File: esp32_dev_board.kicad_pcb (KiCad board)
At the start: 4 copper layers, 26.4 x 67.6 mm, 27 parts, among them J1 USB_B_Micro, J2 Conn_01x12, J3 Conn_01x12, Q1 Q_PMOS_GSD, Q2 MBT3904DW1, SW1 SW_Push, U1 ESP32-WROOM-32, U2 AP2112K-3.3, U3 FT231XS

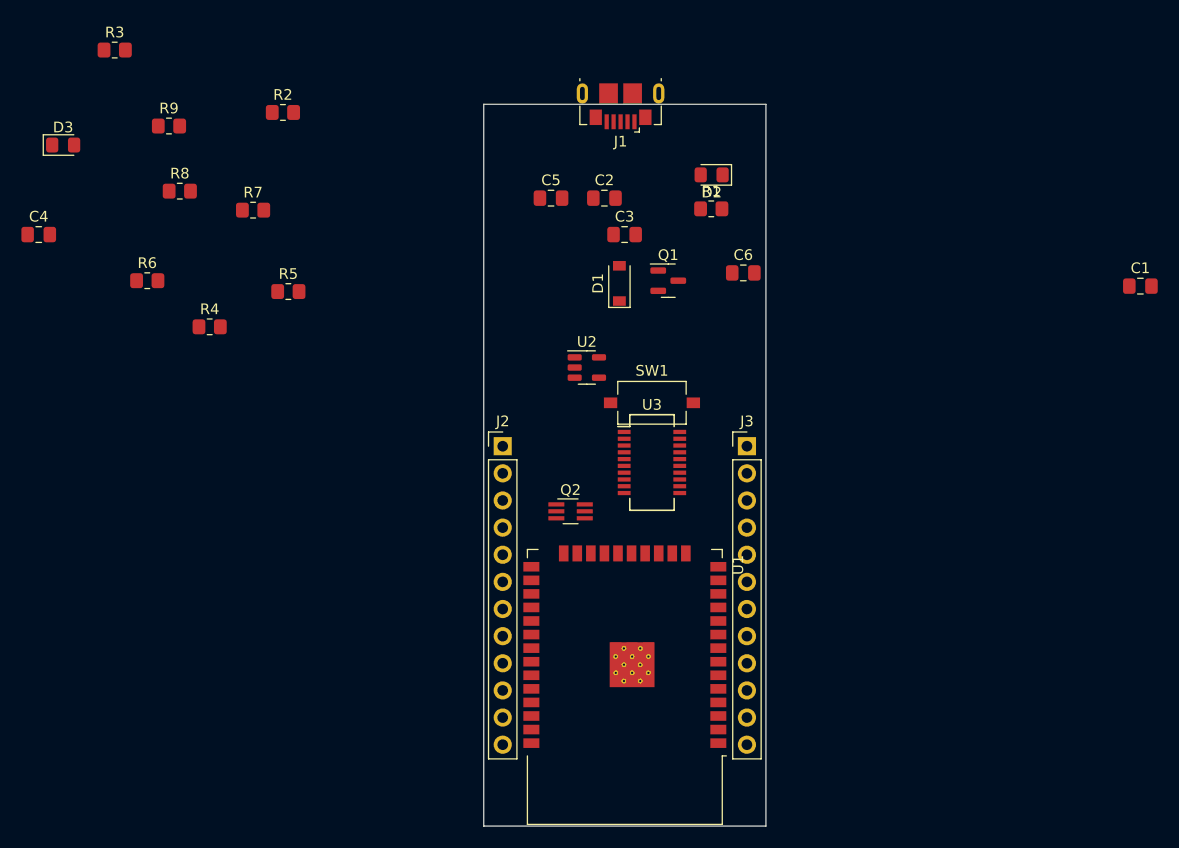
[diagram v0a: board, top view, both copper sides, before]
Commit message: Change to 4-layer board and finish routing
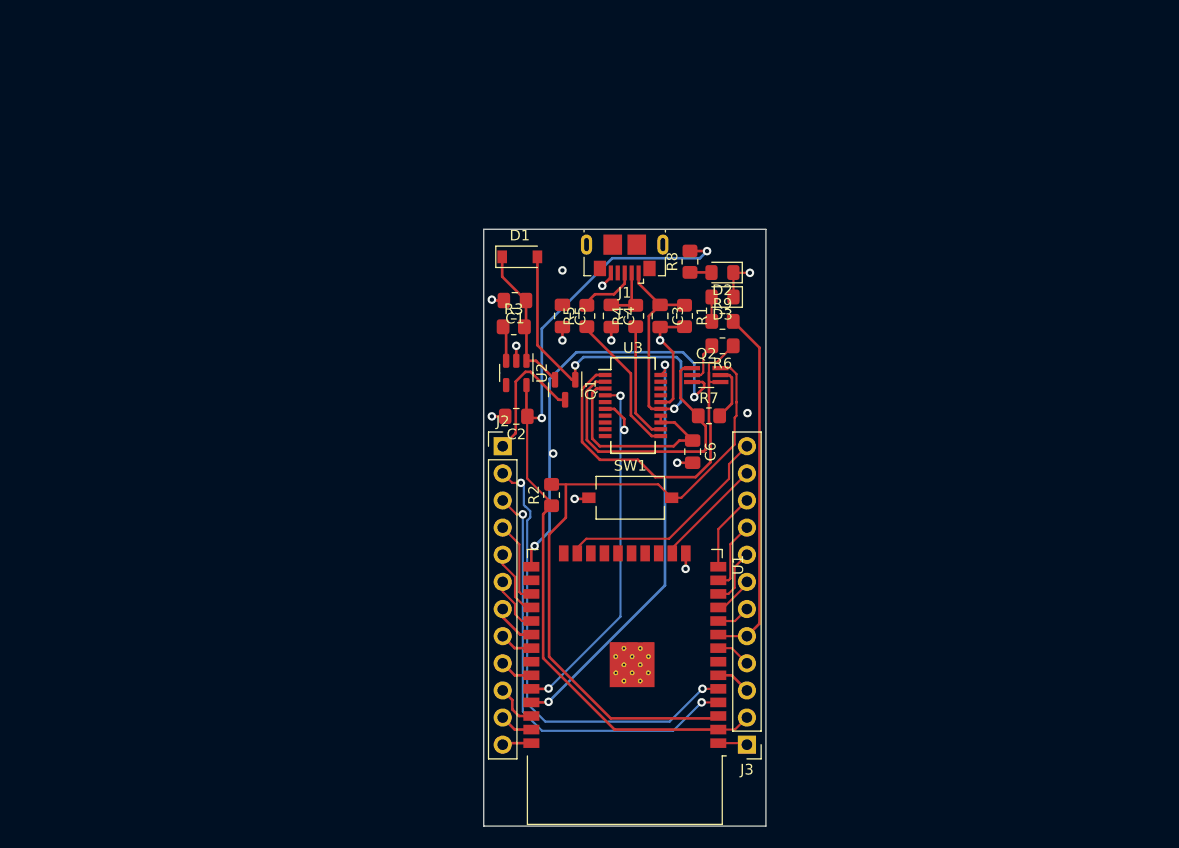
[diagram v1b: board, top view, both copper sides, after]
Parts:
- moved D3 63.3 mm to (178.1, 95.2), turned to 180 degrees
- moved C1 58.6 mm to (158.6, 95.6), turned to 180 degrees
- moved R9 54.9 mm to (178.1, 97.5)
- moved R6 54.2 mm to (178.1, 99.8), turned to 180 degrees
- moved C4 54.1 mm to (167.6, 97.0), turned to -90 degrees
- moved R8 48.2 mm to (175.0, 91.9), turned to 90 degrees
- moved R7 46.8 mm to (176.8, 106.4)
- moved R3 45.5 mm to (158.5, 98.0)
- moved R2 43.8 mm to (162.1, 113.8), turned to 90 degrees
- moved R4 39.9 mm to (169.9, 97.0), turned to 90 degrees
- moved R5 28.0 mm to (165.4, 97.0), turned to 90 degrees
- moved J3 27.9 mm to (180.3, 137.2), turned to 180 degrees
- moved C2 22.0 mm to (158.8, 106.4), turned to 180 degrees
- moved Q2 18.0 mm to (176.5, 102.6)
- moved C6 17.4 mm to (175.3, 109.7), turned to -90 degrees
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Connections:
- U3 pad 20: TX -> TX0
- U3 pad 4: RX -> RX0
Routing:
- net +3.3V: track 0.00 -> 79.0 mm, vias 0 -> 2
- net CHIP_PU: track 0.00 -> 63.3 mm
- net VBUS: track 0.00 -> 48.1 mm, vias 0 -> 2
- net A3: track 0.00 -> 43.1 mm, vias 0 -> 2
- net A4: track 0.00 -> 41.0 mm, vias 0 -> 2
- net GPIO0: track 0.00 -> 39.3 mm, vias 0 -> 2
- net TX0: track 0.00 -> 38.8 mm, vias 0 -> 2
- net DTR: track 0.00 -> 35.8 mm
- net GND: track 0.00 -> 35.5 mm, vias 0 -> 15
- net GPIO33: track 0.00 -> 33.7 mm
- net RX0: track 0.00 -> 33.3 mm, vias 0 -> 2
- net RTS: track 0.00 -> 27.8 mm
- net MTDO: track 0.00 -> 21.2 mm
- net Net-(C6-Pad1): track 0.00 -> 19.9 mm
- net Net-(C1-Pad1): track 0.00 -> 14.2 mm
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- added copper zone on In1.Cu, net GND
- added copper zone on In2.Cu, net GND
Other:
- board size 26.4 x 67.6 mm -> 26.4 x 55.9 mm

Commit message: Add silkscreen, round corners, and small fixes
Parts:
- added C7: 1uF, Capacitor_SMD:C_0805_2012Metric_Pad1.18x1.45mm_HandSolder, F.Cu at (162.7, 109.4)
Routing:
- net VIN: track 12.6 -> 16.4 mm
- net GND: track 35.5 -> 37.9 mm, vias 15 -> 27
- net Net-(C5-Pad1): track 5.54 -> 7.84 mm
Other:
- board size 26.4 x 55.9 mm -> 25.9 x 55.9 mm
- board text added: "+3.3V"
- board text added: "21"
- board text added: "27"
- board text added: "32"
- board text added: "33"
- board text added: "A0"
- board text added: "A1"
- board text added: "A2"
- board text added: "A3"
- board text added: "A4"
- board text added: "GND"
- board text added: "MISO"
- board text added: "MOSI"
- board text added: "MTCK"
- board text added: "MTDI"
- board text added: "MTDO"
- board text added: "MTMS"
- board text added: "RX2"
- board text added: "SCK"
- board text added: "SCL"
- board text added: "SDA"
- board text added: "TX2"
- board text added: "VIN"

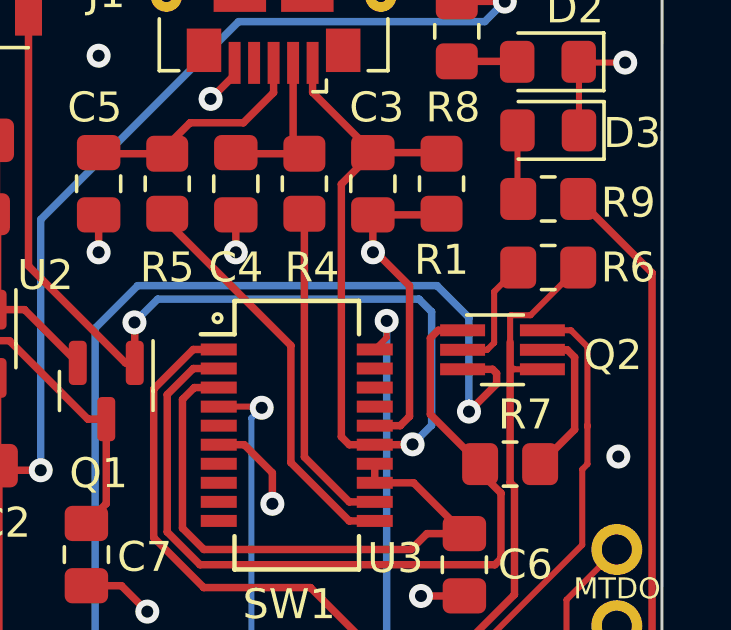
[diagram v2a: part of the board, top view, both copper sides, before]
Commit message: Change C2 value and add back silkscreen
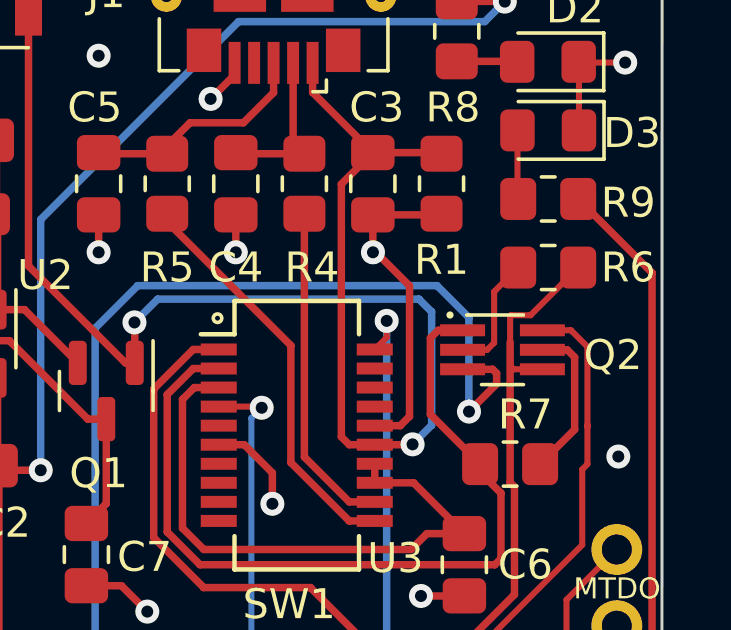
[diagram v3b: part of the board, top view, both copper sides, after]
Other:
- board text added: "Noah White ESP32 Dev Board Rev 1.0"
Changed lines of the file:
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@@
     )
   )
-  (footprint "Package_TO_SOT_SMD:SOT-363_SC-70-6_Handsoldering" placed (layer "F.Cu")
+  (footprint "Package_TO_SOT_SMD:SOT-363_SC-70-6_Handsoldering" (layer "F.Cu")
     (at 176.53 102.563413)
     (descr "SOT-363, SC-70-6, Handsoldering")
@@
       (effects (font (size 0.5 0.5) (thickness 0.075)))
     )
+    (fp_line (start -0.7 1.16) (end 0.7 1.16) (layer "F.SilkS") (width 0.12))
     (fp_line (start 0.7 -1.16) (end -1.2 -1.16) (layer "F.SilkS") (width 0.12))
-    (fp_line (start -0.7 1.16) (end 0.7 1.16) (layer "F.SilkS") (width 0.12))
+    (fp_circle (center -1.75 -1.16) (end -1.69 -1.16) (layer "F.SilkS") (width 0.12) (fill none))
+    (fp_line (start -2.4 -1.4) (end 2.4 -1.4) (layer "F.CrtYd") (width 0.05))
     (fp_line (start -2.4 1.4) (end 2.4 1.4) (layer "F.CrtYd") (width 0.05))
+    (fp_line (start -2.4 -1.4) (end -2.4 1.4) (layer "F.CrtYd") (width 0.05))
     (fp_line (start 2.4 1.4) (end 2.4 -1.4) (layer "F.CrtYd") (width 0.05))
-    (fp_line (start -2.4 -1.4) (end 2.4 -1.4) (layer "F.CrtYd") (width 0.05))
-    (fp_line (start -2.4 -1.4) (end -2.4 1.4) (layer "F.CrtYd") (width 0.05))
+    (fp_line (start -0.675 -0.6) (end -0.675 1.1) (layer "F.Fab") (width 0.1))
     (fp_line (start 0.675 1.1) (end -0.675 1.1) (layer "F.Fab") (width 0.1))
-    (fp_line (start -0.675 -0.6) (end -0.675 1.1) (layer "F.Fab") (width 0.1))
+    (fp_line (start -0.175 -1.1) (end -0.675 -0.6) (layer "F.Fab") (width 0.1))
+    (fp_line (start 0.675 -1.1) (end -0.175 -1.1) (layer "F.Fab") (width 0.1))
     (fp_line (start 0.675 -1.1) (end 0.675 1.1) (layer "F.Fab") (width 0.1))
-    (fp_line (start 0.675 -1.1) (end -0.175 -1.1) (layer "F.Fab") (width 0.1))
-    (fp_line (start -0.175 -1.1) (end -0.675 -0.6) (layer "F.Fab") (width 0.1))
     (pad "1" smd rect (at -1.33 -0.65) (size 1.5 0.4) (layers "F.Cu" "F.Paste" "F.Mask")
       (net 33 "RTS") (pinfunction "E1") (pintype "passive"))
@@
   (gr_line (start 155.968 143.287) (end 157.486 144.773) (layer "Edge.Cuts") (width 0.1))
   (gr_line (start 155.968 143.287) (end 155.984 90.425) (layer "Edge.Cuts") (width 0.1))
+  (gr_text "Noah White\nESP32 Dev Board\nRev 1.0" (at 162.375 124.175 90) (layer "B.SilkS")
+    (effects (font (size 1 1) (thickness 0.15)) (justify mirror))
+  )
   (gr_text "A4" (at 157.475 115.6) (layer "F.SilkS")
     (effects (font (size 0.7 0.7) (thickness 0.1)))

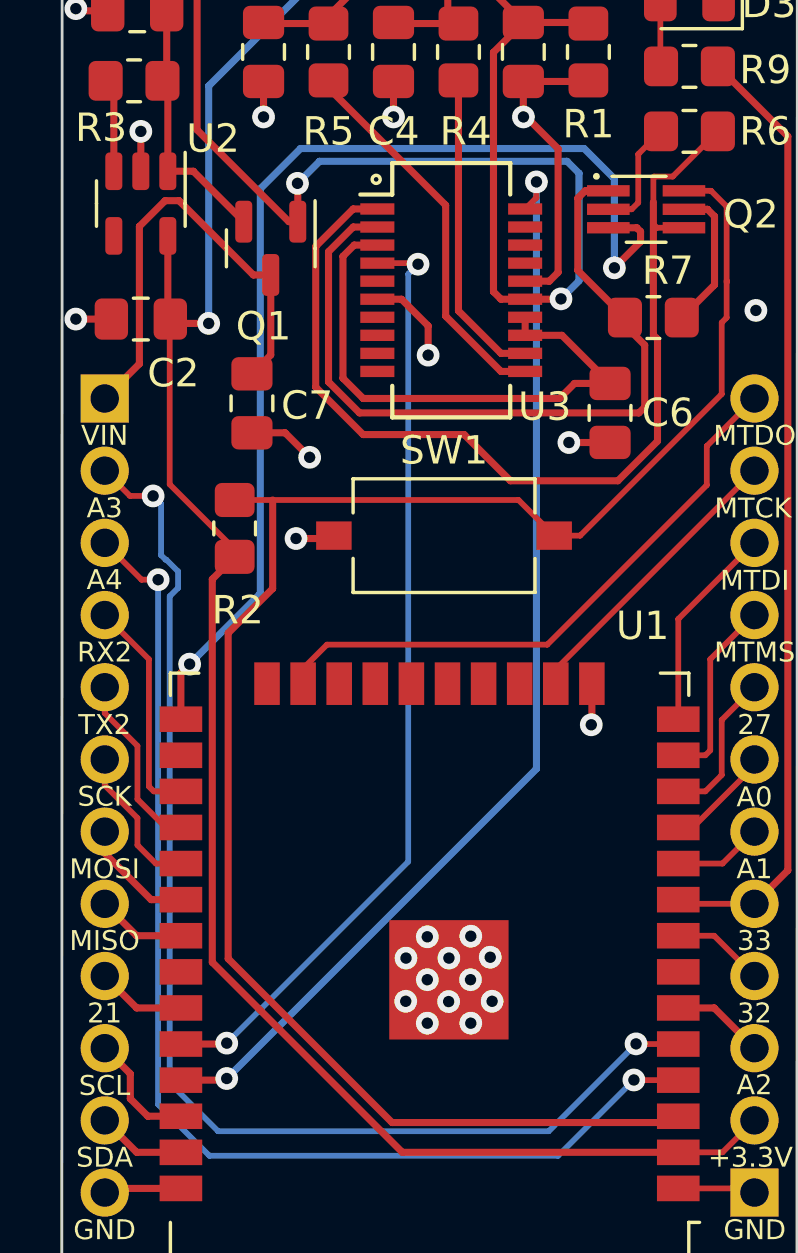
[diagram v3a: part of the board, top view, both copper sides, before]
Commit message: Fix serial connection between ESP32 and FT231X
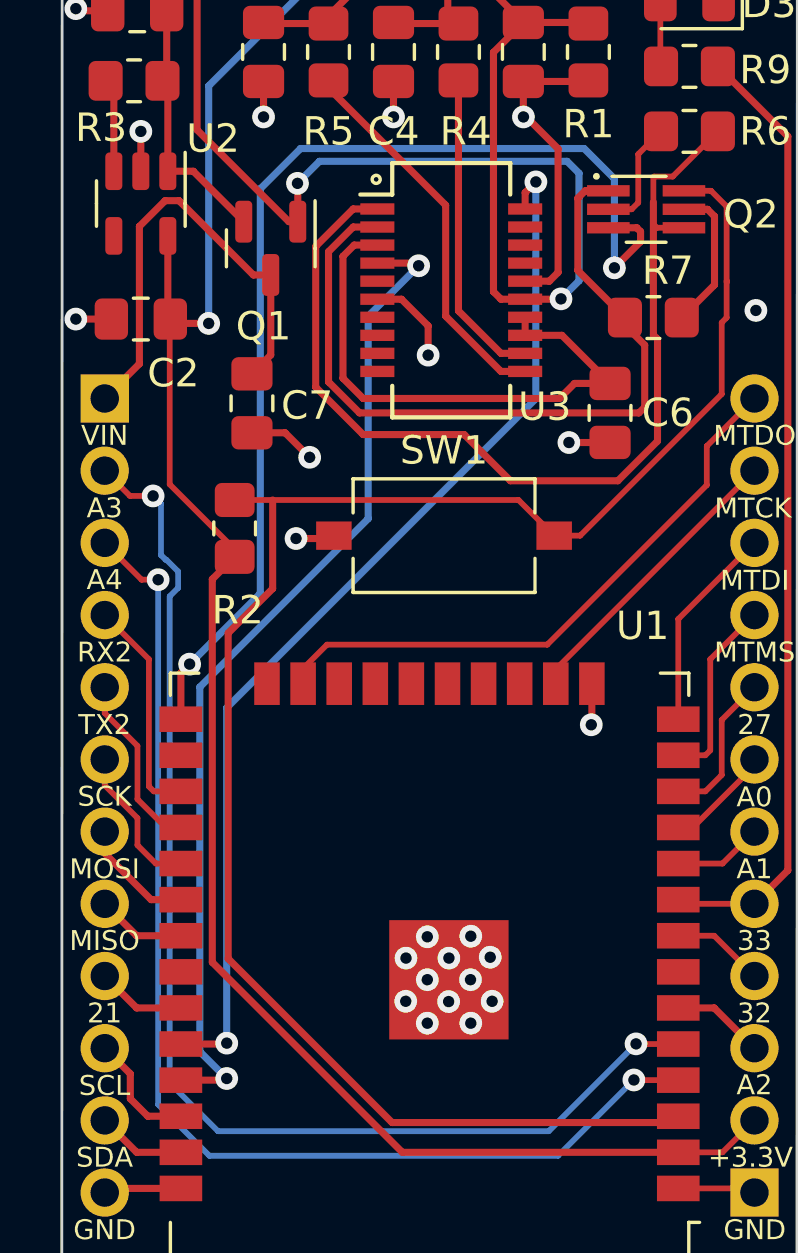
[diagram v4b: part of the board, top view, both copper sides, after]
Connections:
- U3 pad 20: TX0 -> RX0
- U3 pad 4: RX0 -> TX0
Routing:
- net RX0: track 33.3 -> 37.5 mm
- net TX0: track 38.8 -> 35.3 mm
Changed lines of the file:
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@@
       (net 7 "Net-(C6-Pad1)") (pinfunction "VCCIO") (pintype "power_in"))
     (pad "4" smd rect (at -2.6 -0.9525) (size 1.2 0.4) (layers "F.Cu" "F.Paste" "F.Mask")
-      (net 52 "RX0") (pinfunction "RXD") (pintype "input"))
+      (net 53 "TX0") (pinfunction "RXD") (pintype "input"))
     (pad "5" smd rect (at -2.6 -0.3175) (size 1.2 0.4) (layers "F.Cu" "F.Paste" "F.Mask")
       (net 55 "unconnected-(U3-Pad5)") (pinfunction "~{RI}") (pintype "input+no_connect"))
@@
       (net 62 "unconnected-(U3-Pad19)") (pinfunction "CBUS3") (pintype "bidirectional+no_connect"))
     (pad "20" smd rect (at 2.6 -2.8575) (size 1.2 0.4) (layers "F.Cu" "F.Paste" "F.Mask")
-      (net 53 "TX0") (pinfunction "TXD") (pintype "output"))
+      (net 52 "RX0") (pinfunction "TXD") (pintype "output"))
     (model "${KICAD6_3DMODEL_DIR}/Package_SO.3dshapes/SSOP-20_3.9x8.7mm_P0.635mm.wrl"
       (offset (xyz 0 0 0))
@@
   (segment (start 165.354 98.298) (end 165.354 98.028) (width 0.25) (layer "F.Cu") (net 41))
   (segment (start 160.16 131.9338) (end 161.741 131.9338) (width 0.25) (layer "F.Cu") (net 52))
-  (segment (start 167.072 104.4575) (end 168.4655 104.4575) (width 0.2032) (layer "F.Cu") (net 52))
-  (segment (start 168.4655 104.4575) (end 168.5036 104.4956) (width 0.2032) (layer "F.Cu") (net 52))
+  (segment (start 172.272 101.978) (end 172.65 101.6) (width 0.25) (layer "F.Cu") (net 52))
   (segment (start 161.741 131.9338) (end 161.7726 131.9022) (width 0.25) (layer "F.Cu") (net 52))
-  (via (at 168.5036 104.4956) (size 0.8) (drill 0.4) (layers "F.Cu" "B.Cu") (free) (net 52))
+  (segment (start 172.272 102.5525) (end 172.272 101.978) (width 0.25) (layer "F.Cu") (net 52))
+  (via (at 172.65 101.6) (size 0.8) (drill 0.4) (layers "F.Cu" "B.Cu") (free) (net 52))
   (via (at 161.7726 131.9022) (size 0.8) (drill 0.4) (layers "F.Cu" "B.Cu") (free) (net 52))
-  (segment (start 168.1576 125.5172) (end 161.7726 131.9022) (width 0.2032) (layer "B.Cu") (net 52))
-  (segment (start 168.1576 104.8416) (end 168.1576 125.5172) (width 0.2032) (layer "B.Cu") (net 52))
-  (segment (start 168.5036 104.4956) (end 168.1576 104.8416) (width 0.2032) (layer "B.Cu") (net 52))
+  (segment (start 161.7726 131.9022) (end 161.7726 120.1024) (width 0.25) (layer "B.Cu") (net 52))
+  (segment (start 161.7726 120.1024) (end 172.65 109.225) (width 0.25) (layer "B.Cu") (net 52))
+  (segment (start 172.65 109.225) (end 172.65 101.6) (width 0.25) (layer "B.Cu") (net 52))
   (segment (start 160.16 133.2038) (end 161.7156 133.2038) (width 0.25) (layer "F.Cu") (net 53))
-  (segment (start 172.6692 101.5995) (end 172.6692 102.1553) (width 0.2032) (layer "F.Cu") (net 53))
-  (segment (start 172.6692 102.1553) (end 172.272 102.5525) (width 0.2032) (layer "F.Cu") (net 53))
+  (segment (start 167.072 104.4575) (end 168.4325 104.4575) (width 0.25) (layer "F.Cu") (net 53))
+  (segment (start 168.4325 104.4575) (end 168.525 104.55) (width 0.25) (layer "F.Cu") (net 53))
   (segment (start 161.7156 133.2038) (end 161.7726 133.1468) (width 0.25) (layer "F.Cu") (net 53))
   (via (at 161.7726 133.1468) (size 0.8) (drill 0.4) (layers "F.Cu" "B.Cu") (free) (net 53))
-  (via (at 172.6692 101.5995) (size 0.8) (drill 0.4) (layers "F.Cu" "B.Cu") (free) (net 53))
-  (segment (start 172.6692 101.5995) (end 172.6692 122.2502) (width 0.25) (layer "B.Cu") (net 53))
-  (segment (start 172.6692 122.2502) (end 161.7726 133.1468) (width 0.25) (layer "B.Cu") (net 53))
+  (via (at 168.525 104.55) (size 0.8) (drill 0.4) (layers "F.Cu" "B.Cu") (free) (net 53))
+  (segment (start 161.7726 133.1468) (end 160.825 132.1992) (width 0.25) (layer "B.Cu") (net 53))
+  (segment (start 166.75 106.325) (end 168.525 104.55) (width 0.25) (layer "B.Cu") (net 53))
+  (segment (start 160.825 132.1992) (end 160.825 119.375) (width 0.25) (layer "B.Cu") (net 53))
+  (segment (start 160.825 119.375) (end 166.75 113.45) (width 0.25) (layer "B.Cu") (net 53))
+  (segment (start 166.75 113.45) (end 166.75 106.325) (width 0.25) (layer "B.Cu") (net 53))
   (zone (net 2) (net_name "GND") (layer "In1.Cu") (name "GND") (hatch edge 0.508)
     (connect_pads (clearance 0.508))
